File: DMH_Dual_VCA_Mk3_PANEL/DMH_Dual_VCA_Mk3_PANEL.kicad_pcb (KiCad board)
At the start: 2 copper layers, 50 x 200 mm, 23 parts, among them J0 Panel_GND_Solder_Wire_Pad

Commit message: Started PCB 2 project
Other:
- board text added: "Auto"
- board text added: "Dist"

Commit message: Mode switching design in progress
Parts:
- H20: footprint SynthStuff:Pot_Cutout_Tiny_attv_P110KH1 -> SynthStuff:Pot_Cutout_Tiny_attv_RD901F
- H21: value Pan/Trem -> Mode
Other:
- board text added: "Bal"
- board text removed: "Auto"

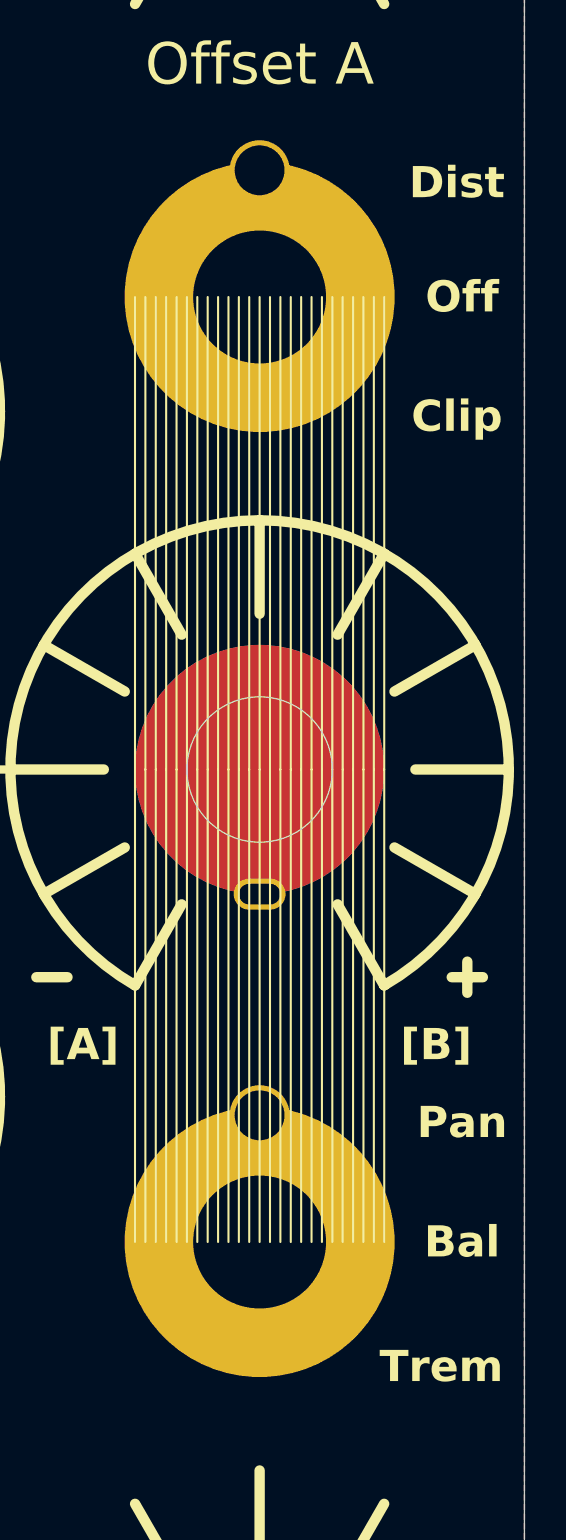
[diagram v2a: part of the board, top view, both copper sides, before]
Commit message: Improved clipping indication
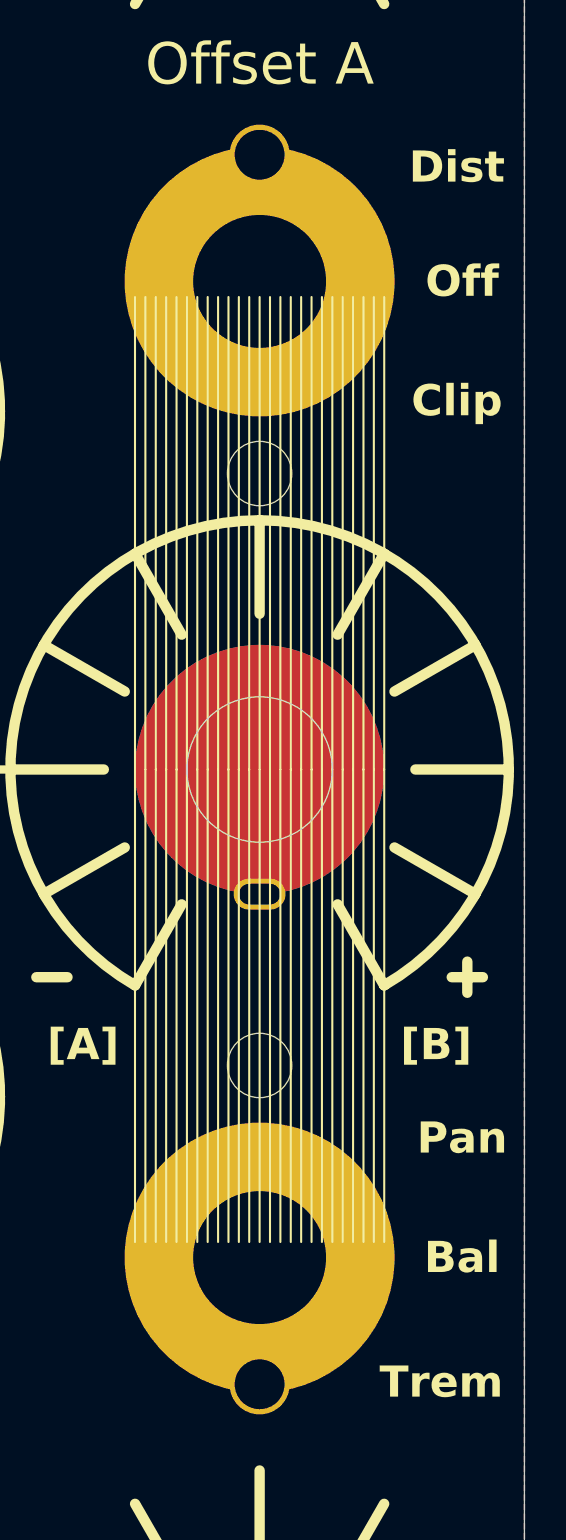
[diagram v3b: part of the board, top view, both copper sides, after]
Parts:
- added H23: LED A, SynthStuff:MountingHole_LED_3mm_R, F.Cu at (87.2, 89.0)
- added H24: LED B, SynthStuff:MountingHole_LED_3mm_R, F.Cu at (87.2, 117.5)
- moved H21 0.75 mm to (87.2, 126.8), turned to 180 degrees
- moved H22 0.75 mm to (87.2, 79.8)

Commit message: Generated Gerbers
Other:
- board text added: "Mk3.0 - June 2026"
- board text removed: "Mk3.0 - XXXXX 2026"
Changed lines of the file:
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@@
 		)
 	)
-	(gr_text "Mk3.0 - XXXXX 2026"
+	(gr_text "Mk3.0 - June 2026"
 		(at 75 222.95 0)
 		(layer "B.SilkS")
